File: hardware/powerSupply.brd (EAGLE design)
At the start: 100 x 80 mm, 98 parts, among them IC1 MCP3008, IC12 LM358, IC13 LM358, IC2 LM334Z, IC3 MCP4821P, IC4 MCP4821P, IC5 74LS139D, IC6 7805TV, IC7 LP2950Z, IC8 LT3080T, J3 RASPBERRYPI-40-PIN-GPIO_PTH, SW1 EC11B_SW, SW2 EC11B_SW, SW7 B3F-1000, T1 2N3904, T2 2N3904, T3 2N3904, U1 MAX874CPA

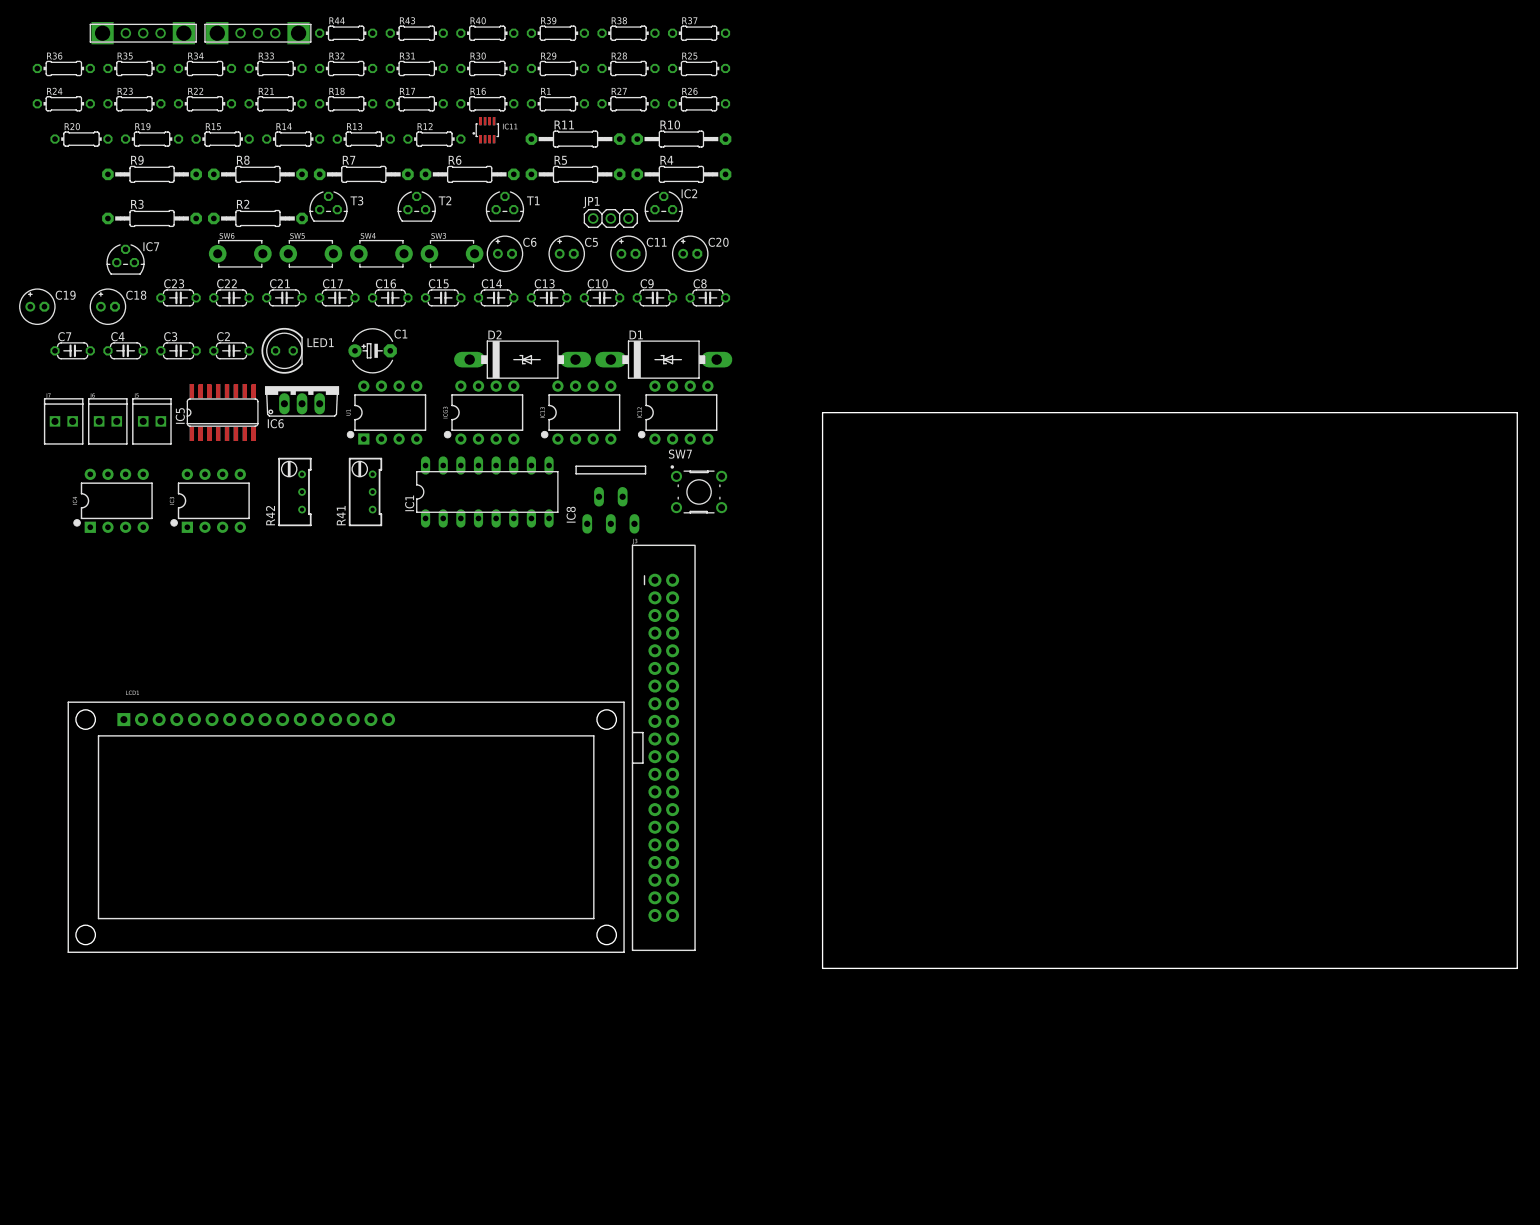
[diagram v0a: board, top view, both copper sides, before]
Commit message: 
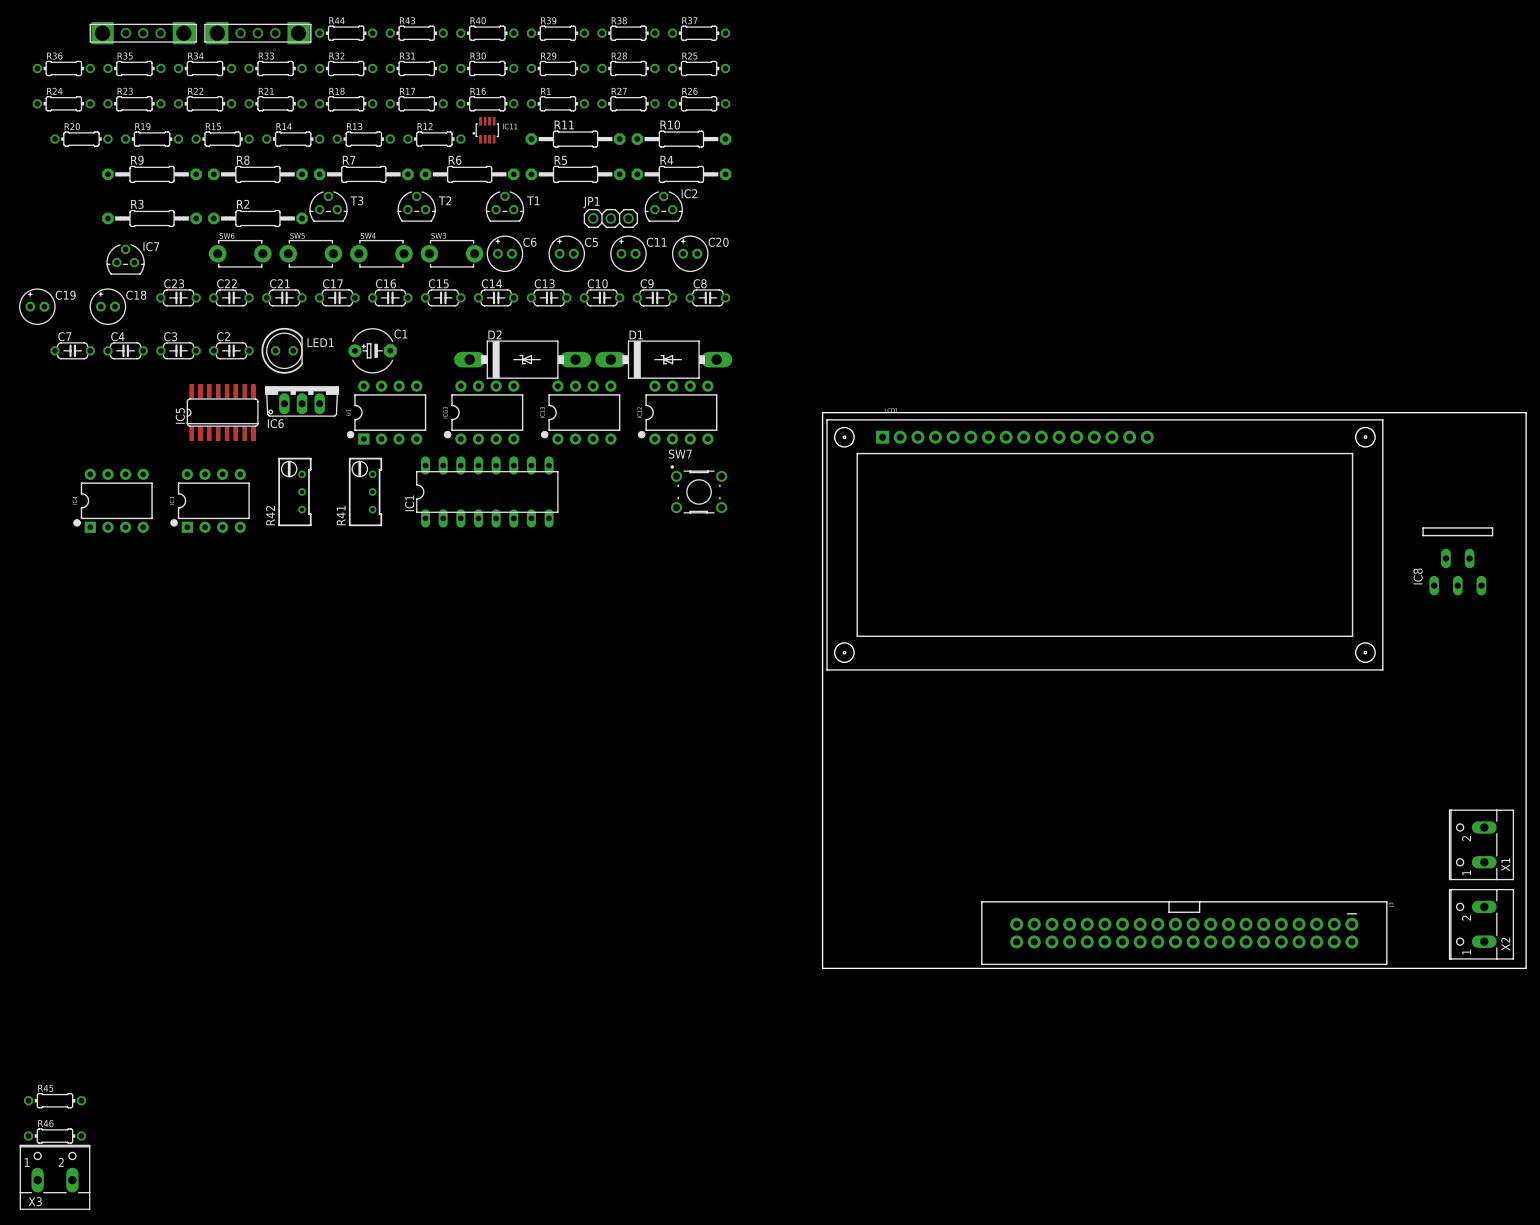
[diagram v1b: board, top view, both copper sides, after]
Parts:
- removed J5, J6, J7: (no value), Hexellence-Connectors:1X02_2.54_SCREWTERM
- added R45, R46: Don't populate, rcl:0204/7
- added X1: VOUT, con-wago-500:W237-102
- added X2: VSENSE, con-wago-500:W237-102
- added X3: VIN, con-wago-500:W237-102
- moved IC8 122.2 mm to (91.4, 63.5)
- moved LCD1 116.5 mm to (40.6, 61.0)
- moved J3 79.5 mm to (52.1, 5.08), turned to 270 degrees
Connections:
- new net N$42: J3.1, J3.17, R45.2
- new net N$44: J3.2, J3.4, R46.2
- net 3.3V: now also R45.1; no longer J3.1, J3.17
- net 5V: now also R46.1; no longer J3.2, J3.4
- net GND: now also X1.2, X2.2, X3.2; no longer J5.P2, J6.P2, J7.P2
- net V+: now also X3.1; no longer J5.P1
- net VOUT: now also X1.1; no longer J6.P1
- net VSENS: now also X2.1; no longer J7.P1
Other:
- board size 100 x 80 mm -> 101.3 x 80 mm

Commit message: 
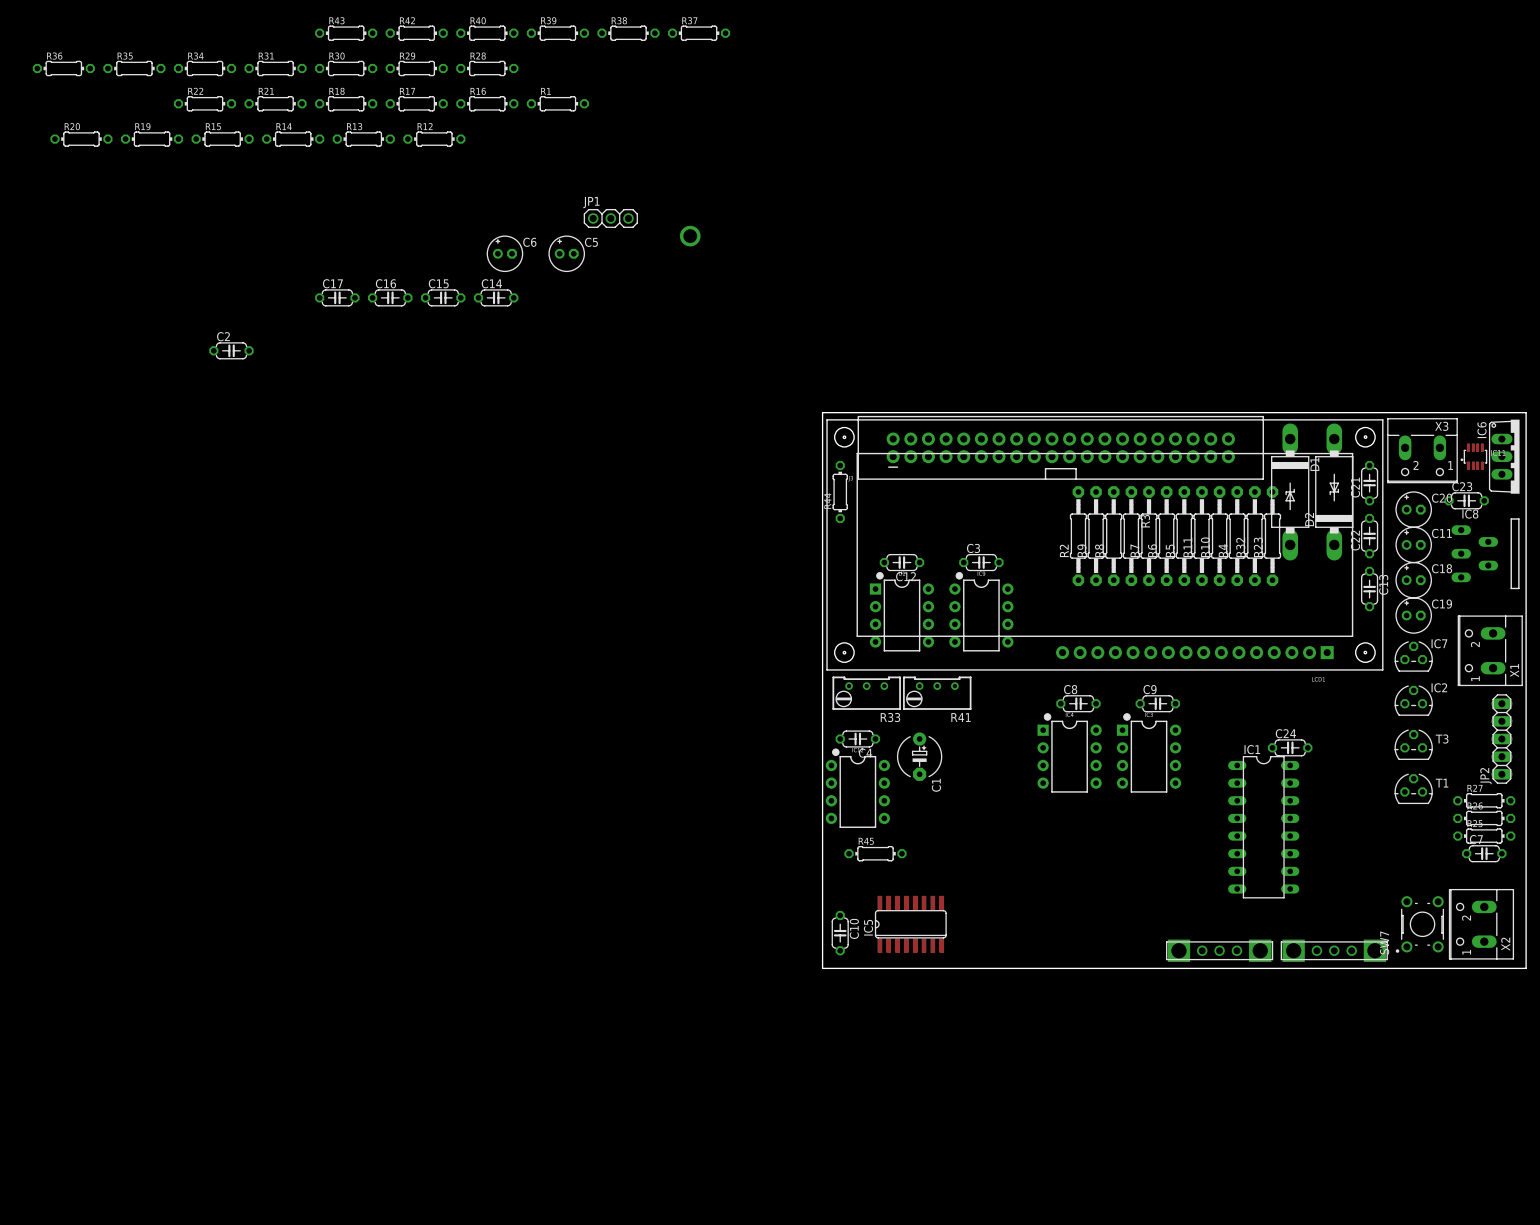
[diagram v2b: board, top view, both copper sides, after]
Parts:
- removed IC13, ICG3: LM358, SparkFun-IC-Amplifiers:DIP08
- removed LED1: (no value), led:LED5MM
- removed R24: 470R, rcl:0204/7
- removed R46: Don't populate, rcl:0204/7
- removed SW3, SW4, SW5, SW6: (no value), adafruit:TACT_PANA-EVQ
- removed T2: 2N3904, transistor:TO92
- added C12, C24: 100n, adafruit:C050-024X044
- added IC9: LM358, SparkFun-IC-Amplifiers:DIP08
- added JP2: (no value), pinhead:1X05
- R23, R32: value 10K -> 10R; device rcl:0204/7 -> adafruit:0207/12
- R28, R29: value 10R -> 10K
- R33: device rcl:0204/7 -> resistor:RTRIM64W
- R42: value 10K -> 2M; device resistor:RTRIM64W -> rcl:0204/7
- R43: value 2M -> 4M
- R44: value 4M -> Don't populate
- moved X3 222.1 mm to (86.4, 73.7), turned to 180 degrees
- moved C7 215.7 mm to (95.2, 16.5)
- moved SW1 203.6 mm to (73.7, 2.54)
- moved SW2 203.6 mm to (57.1, 2.54)
- moved C19 203.0 mm to (85.1, 50.8)
- moved IC7 194.0 mm to (85.1, 44.5)
- moved C18 192.0 mm to (85.1, 55.9)
- moved C23 187.7 mm to (92.7, 67.3)
- moved IC6 175.6 mm to (100.3, 73.7), turned to 270 degrees
- moved R23 175.3 mm to (64.8, 62.2), turned to 90 degrees
- moved T3 174.4 mm to (85.1, 31.8)
- moved C22 167.4 mm to (78.7, 62.2), turned to 90 degrees
- moved R27 158.9 mm to (95.2, 24.1)
- moved C21 158.5 mm to (78.7, 69.8), turned to 90 degrees
- moved R25 158.1 mm to (95.2, 19.1)
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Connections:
- removed net N$15: R23.2, T2.2
- removed net N$16: LED1.K, T2.1
- removed net N$17: LED1.A, R24.1
- net 3.3V: now also R44.1; no longer R45.1
- net 4.096V: now also R42.1; no longer R43.1
- net 5V: now also C12.1, C24.1, R30.1, R31.1, R45.1; no longer R24.2, R32.1, R33.1, R46.1
- net GND: now also C12.2, C24.2, IC9.4, JP2.5, R43.1; no longer ICG3.4, R44.1, SW3.P$2, SW4.P$2, SW5.P$2, SW6.P$2, T2.3
- net N$11: now also IC9.7; no longer IC13.7
- net N$18: now also R33.1; no longer R42.1
- net N$19: now also R32.1; no longer R28.2
- net N$20: now also J3.15; no longer R23.1
- net N$22: now also R28.1, R30.2; no longer R30.1, R32.2
- net N$23: now also R28.2; no longer R30.2
- net N$26: now also R29.2; no longer R31.2
- net N$28: now also R29.1, R31.2; no longer R31.1, R33.2
- net N$3: now also R33.2; no longer R42.2
- net N$30: now also JP2.1; no longer SW3.P$1
- net N$31: now also JP2.2; no longer SW4.P$1
- net N$32: now also JP2.3; no longer SW5.P$1
- net N$33: now also JP2.4; no longer SW6.P$1
- net N$38: now also R33.3; no longer R42.3
- net N$4: now also R23.1; no longer R29.1
- net N$41: now also R42.2; no longer R43.2
- net N$42: now also R44.2; no longer R45.2
- net N$43: now also R43.2; no longer R44.2
- net N$44: now also R45.2; no longer R46.2
- net N$6: now also IC9.1, IC9.2; no longer IC13.1, IC13.2
- net N$7: now also IC9.6; no longer IC13.6
- net N$9: now also IC9.5; no longer IC13.5
- net V+: now also R23.2; no longer R29.2
- net V+1: now also IC9.3, IC9.8, R32.2; no longer IC13.3, ICG3.8, R28.1

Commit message: 
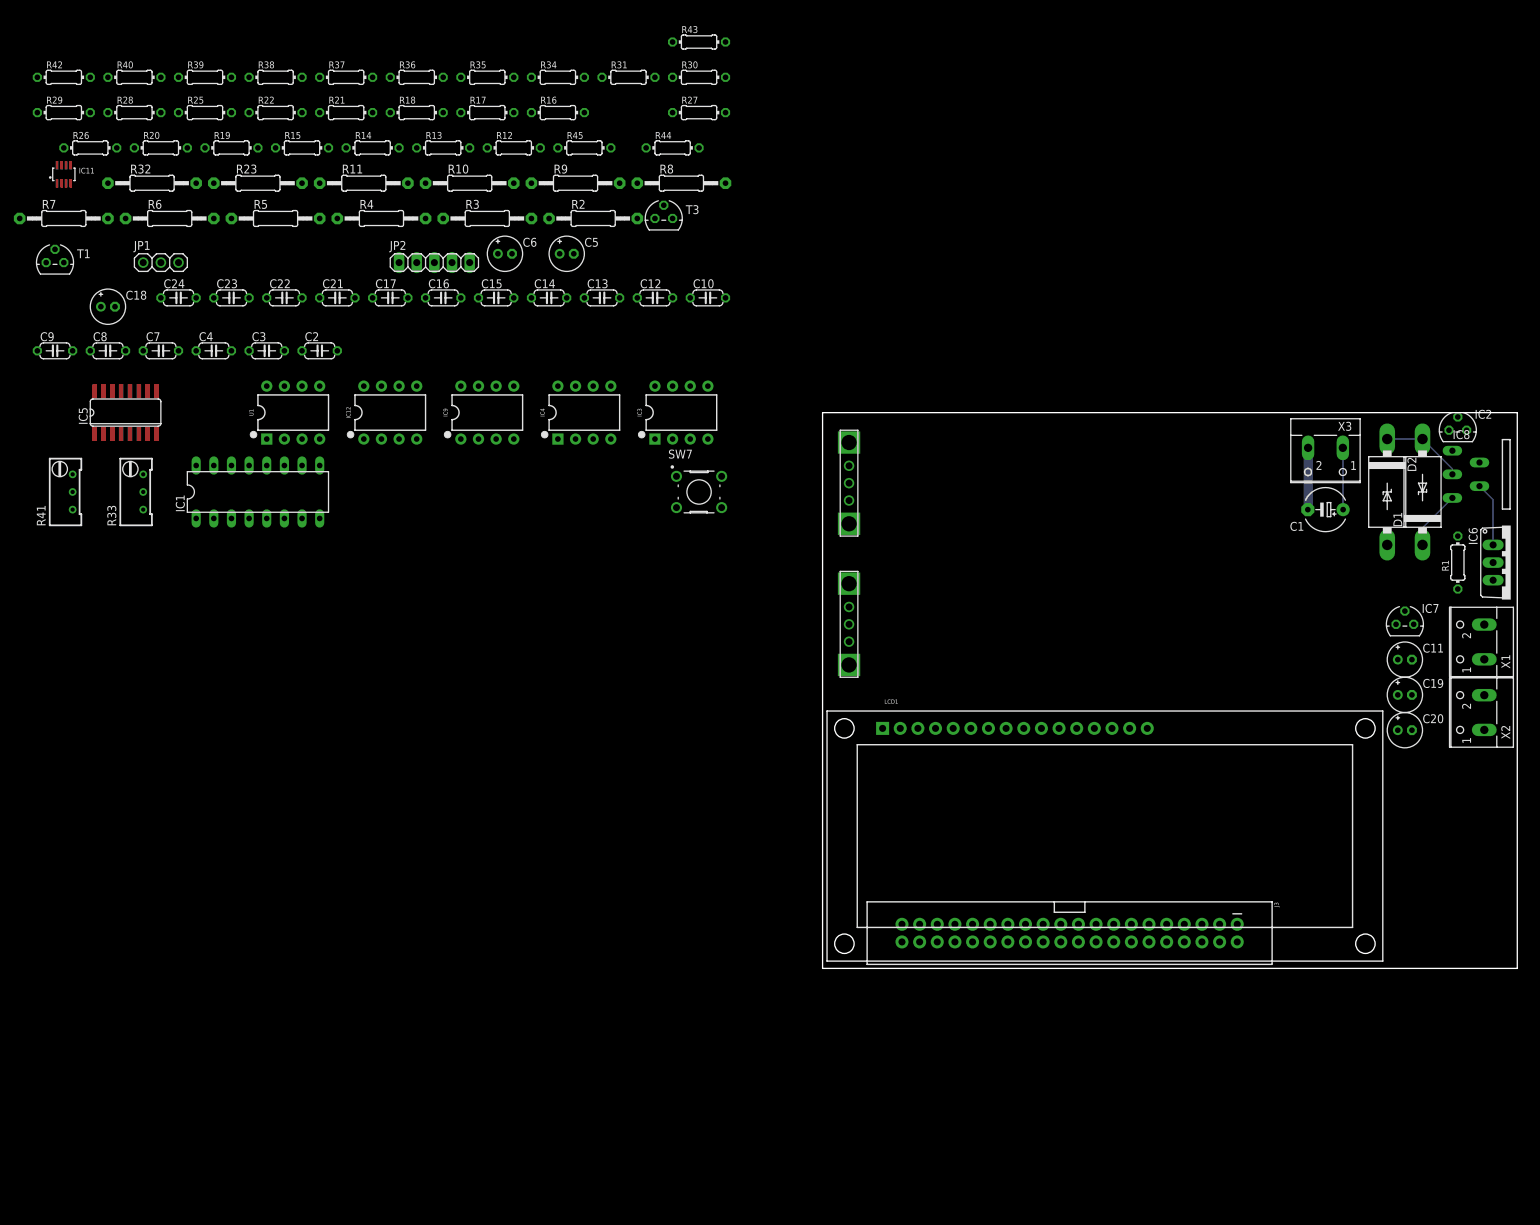
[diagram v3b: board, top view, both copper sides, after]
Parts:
- moved R26 222.7 mm to (-105.4, 118.1)
- moved R25 211.6 mm to (-88.9, 123.2)
- moved T1 209.9 mm to (-110.5, 101.6)
- moved IC11 207.2 mm to (-109.2, 114.3)
- moved C7 203.8 mm to (-95.2, 88.9)
- moved C18 192.0 mm to (-102.9, 95.2)
- moved C23 180.2 mm to (-85.1, 96.5)
- moved C24 172.6 mm to (-92.7, 96.5)
- moved JP2 168.3 mm to (-55.9, 101.6), turned to 0 degrees
- moved C9 166.7 mm to (-110.5, 88.9)
- moved R32 166.7 mm to (-96.5, 113.0), turned to 0 degrees
- moved R7 162.8 mm to (-109.2, 108.0), turned to 0 degrees
- moved C22 159.9 mm to (-77.5, 96.5), turned to 0 degrees
- moved R23 154.6 mm to (-81.3, 113.0), turned to 0 degrees
- moved IC1 152.6 mm to (-81.3, 68.6), turned to 0 degrees
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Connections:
- net V+1 renamed VR
- new net S$1: IC6.1, IC8.4
- net GND: now also X2.1; no longer X1.2, X2.2
- net V+: no longer IC6.1, IC8.4
- net VOUT: now also X1.2
- net VSENS: now also X2.2; no longer X2.1
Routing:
- net VOUT: track 0.00 -> 11.9 mm
- net S$1: track 0.00 -> 9.27 mm
- net GND: track 0.00 -> 8.95 mm
- net V+: track 0.00 -> 8.91 mm
- net VR: track 0.00 -> 8.54 mm
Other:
- board size 101.3 x 80 mm -> 100 x 80 mm
